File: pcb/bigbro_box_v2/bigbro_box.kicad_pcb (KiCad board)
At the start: 2 copper layers, 100 x 58 mm, 44 parts, among them J1 Current Sense, J2 Display, J3 Mains, J4 Debug, J5 RFID, J6 Relay, J7 Ext, K1 G5LE-1, Q1 MMBT3904, Q2 MMBT3904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

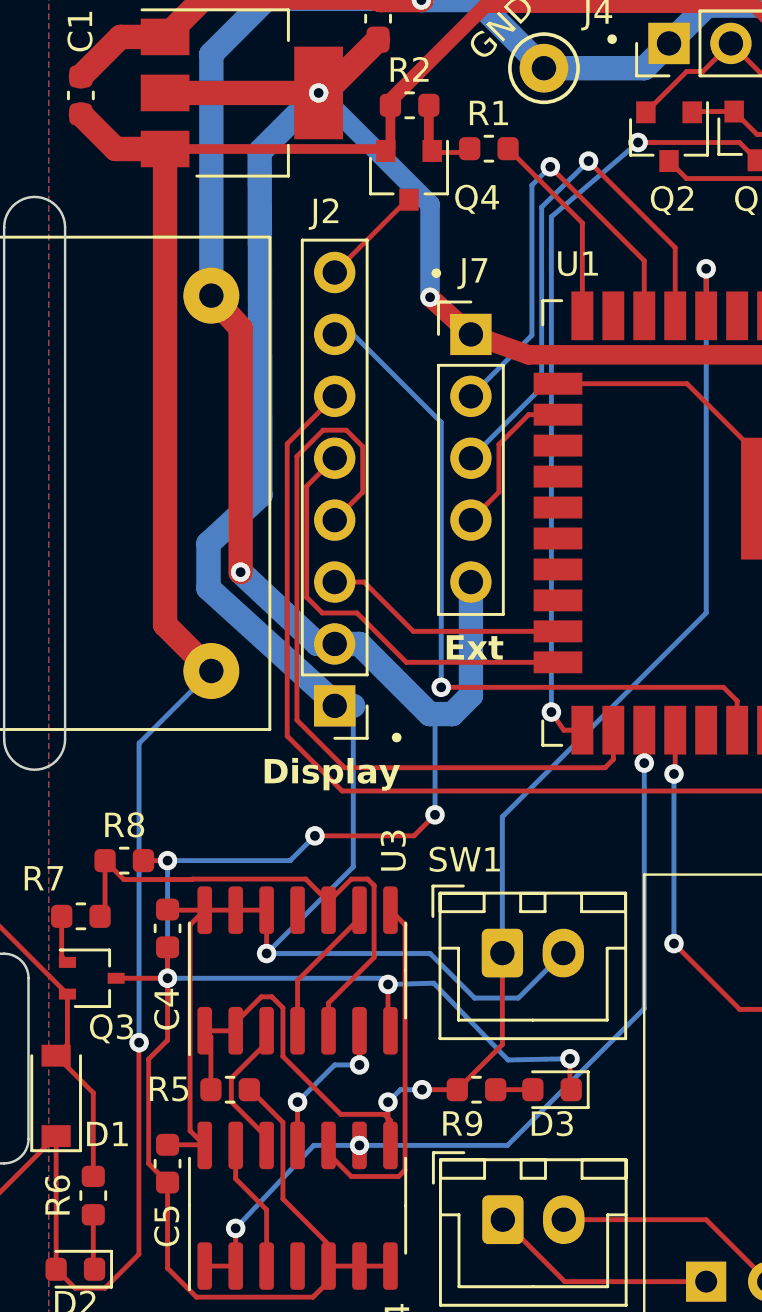
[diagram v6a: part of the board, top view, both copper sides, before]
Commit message: Move display backlight from GPIO12 to GPIO14 to fix boot problem.
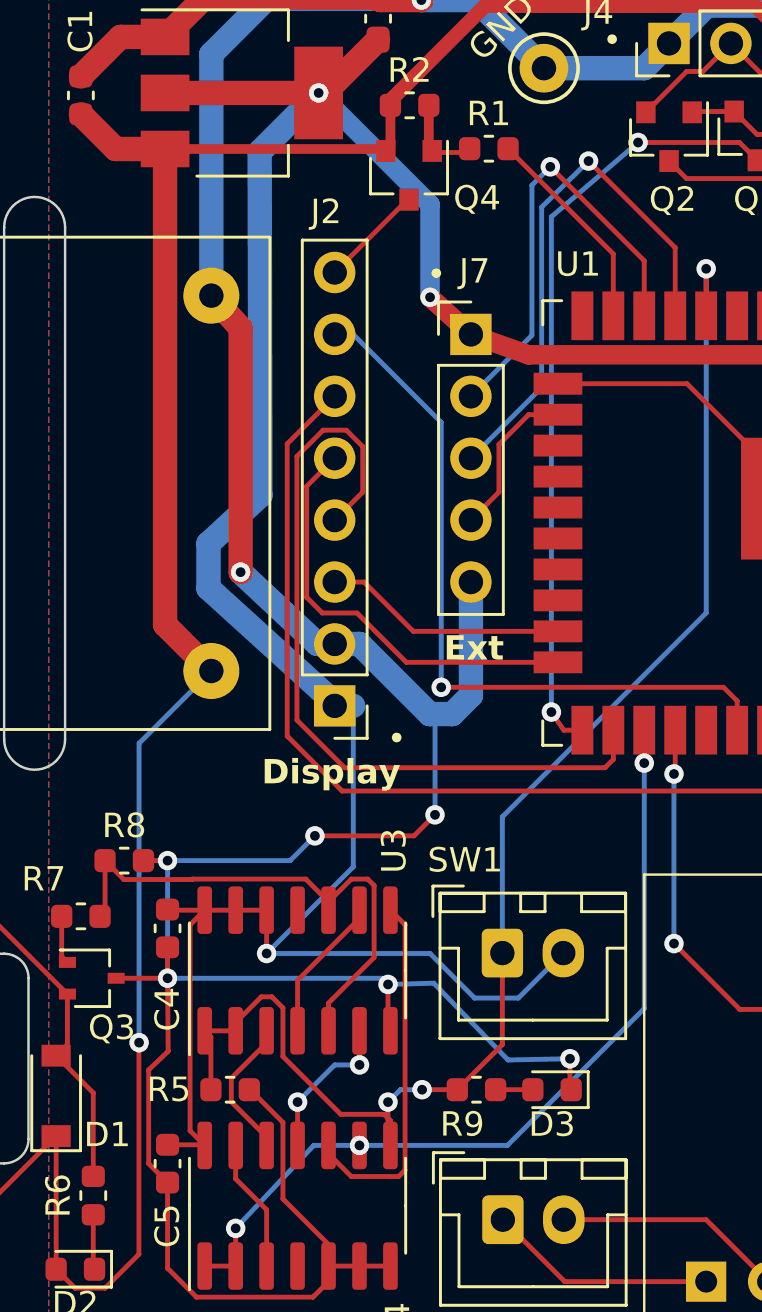
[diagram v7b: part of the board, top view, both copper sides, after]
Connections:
- U1 pad 13: unconnected-(U1-IO14-Pad13) -> Display_backlight
- U1 pad 14: Display_backlight -> unconnected-(U1-IO12-Pad14)
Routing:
- net Display_backlight: track 8.12 -> 8.65 mm

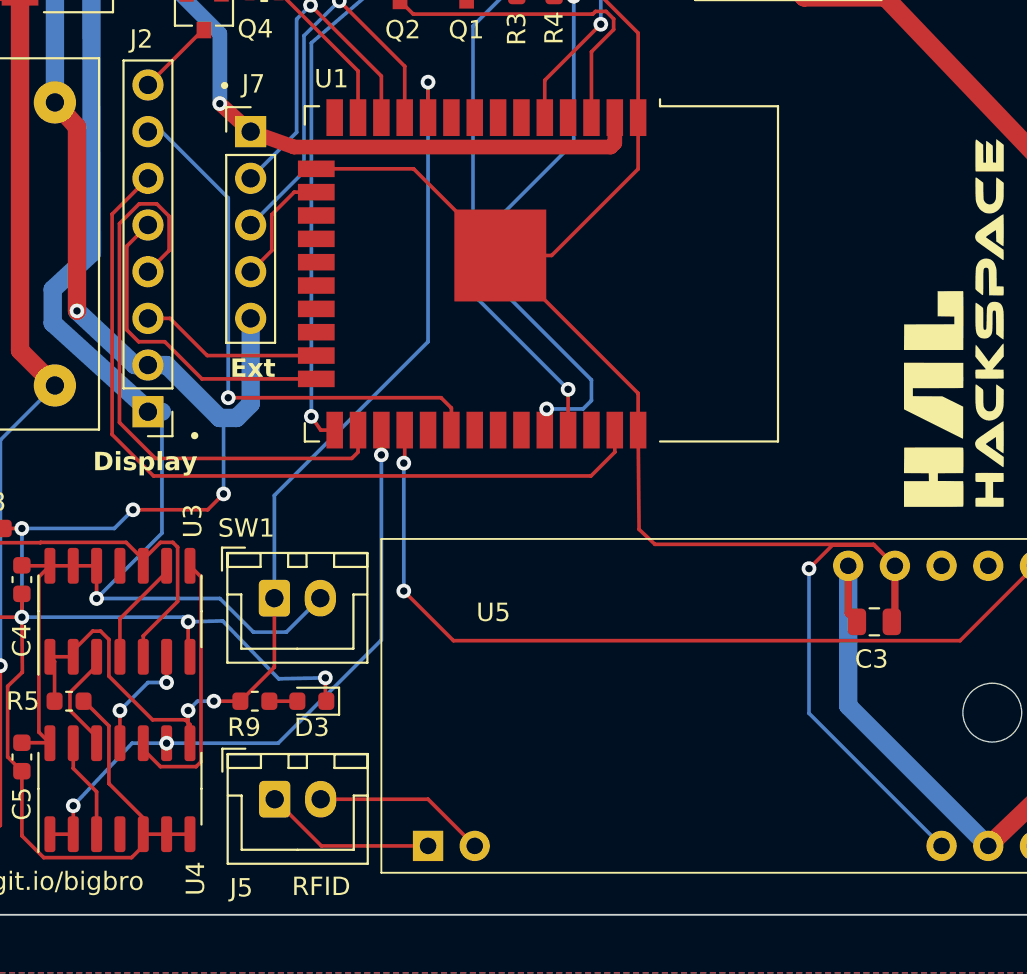
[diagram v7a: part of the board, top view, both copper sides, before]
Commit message: Add reset and boot switches.
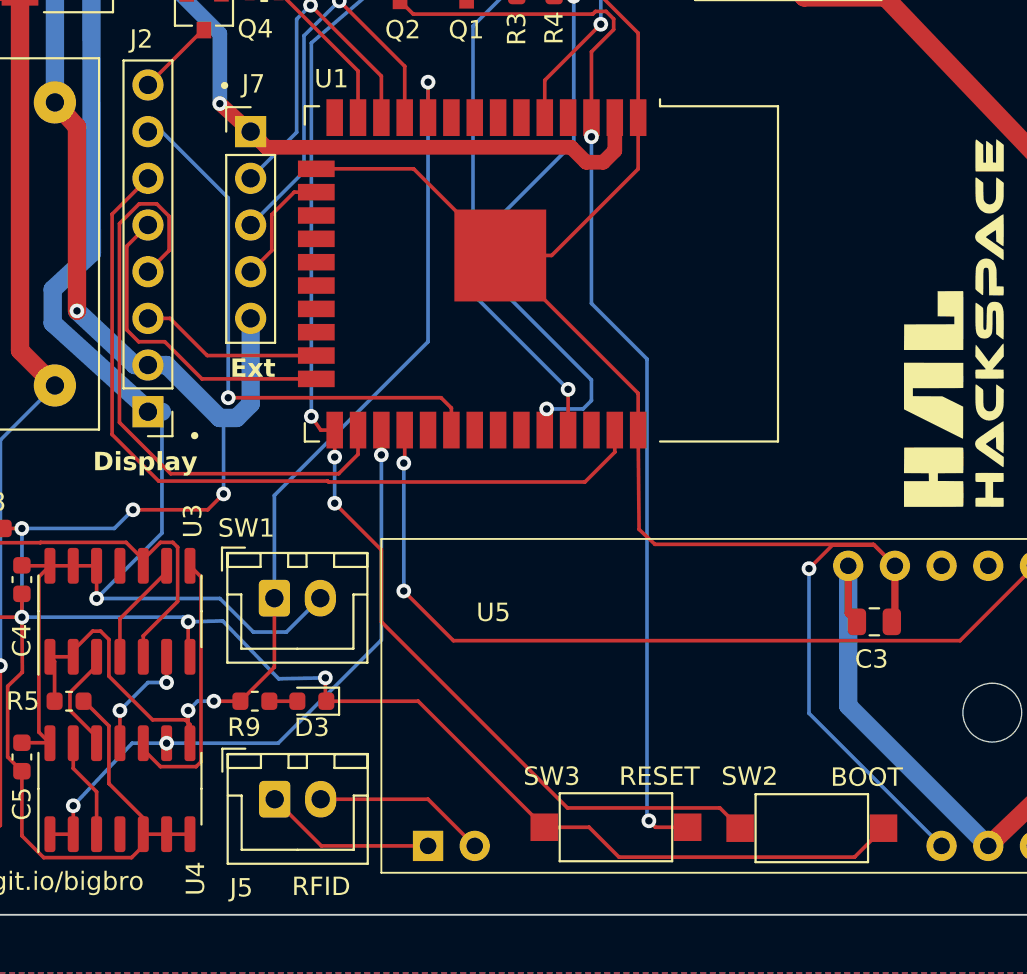
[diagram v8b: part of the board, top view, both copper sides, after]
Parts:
- added SW2: SW_SPST, Button_Switch_SMD:SW_SPST_CK_RS282G05A3, F.Cu at (151.2, 110.3)
- added SW3: SW_SPST, Button_Switch_SMD:SW_SPST_CK_RS282G05A3, F.Cu at (140.5, 110.2)
- R6: value 1K -> 1K5
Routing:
- net /~{RESET}: track 18.0 -> 59.8 mm, vias 0 -> 2
- net /~{BOOT}: track 31.9 -> 67.5 mm, vias 2 -> 4
- net GND: track 282.9 -> 317.4 mm
- net +3V3: track 116.5 -> 117.7 mm
- net Display_Reset: track 32.9 -> 33.6 mm
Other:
- board text added: "BOOT"
- board text added: "RESET"
